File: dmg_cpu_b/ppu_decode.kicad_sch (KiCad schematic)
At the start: 39 parts

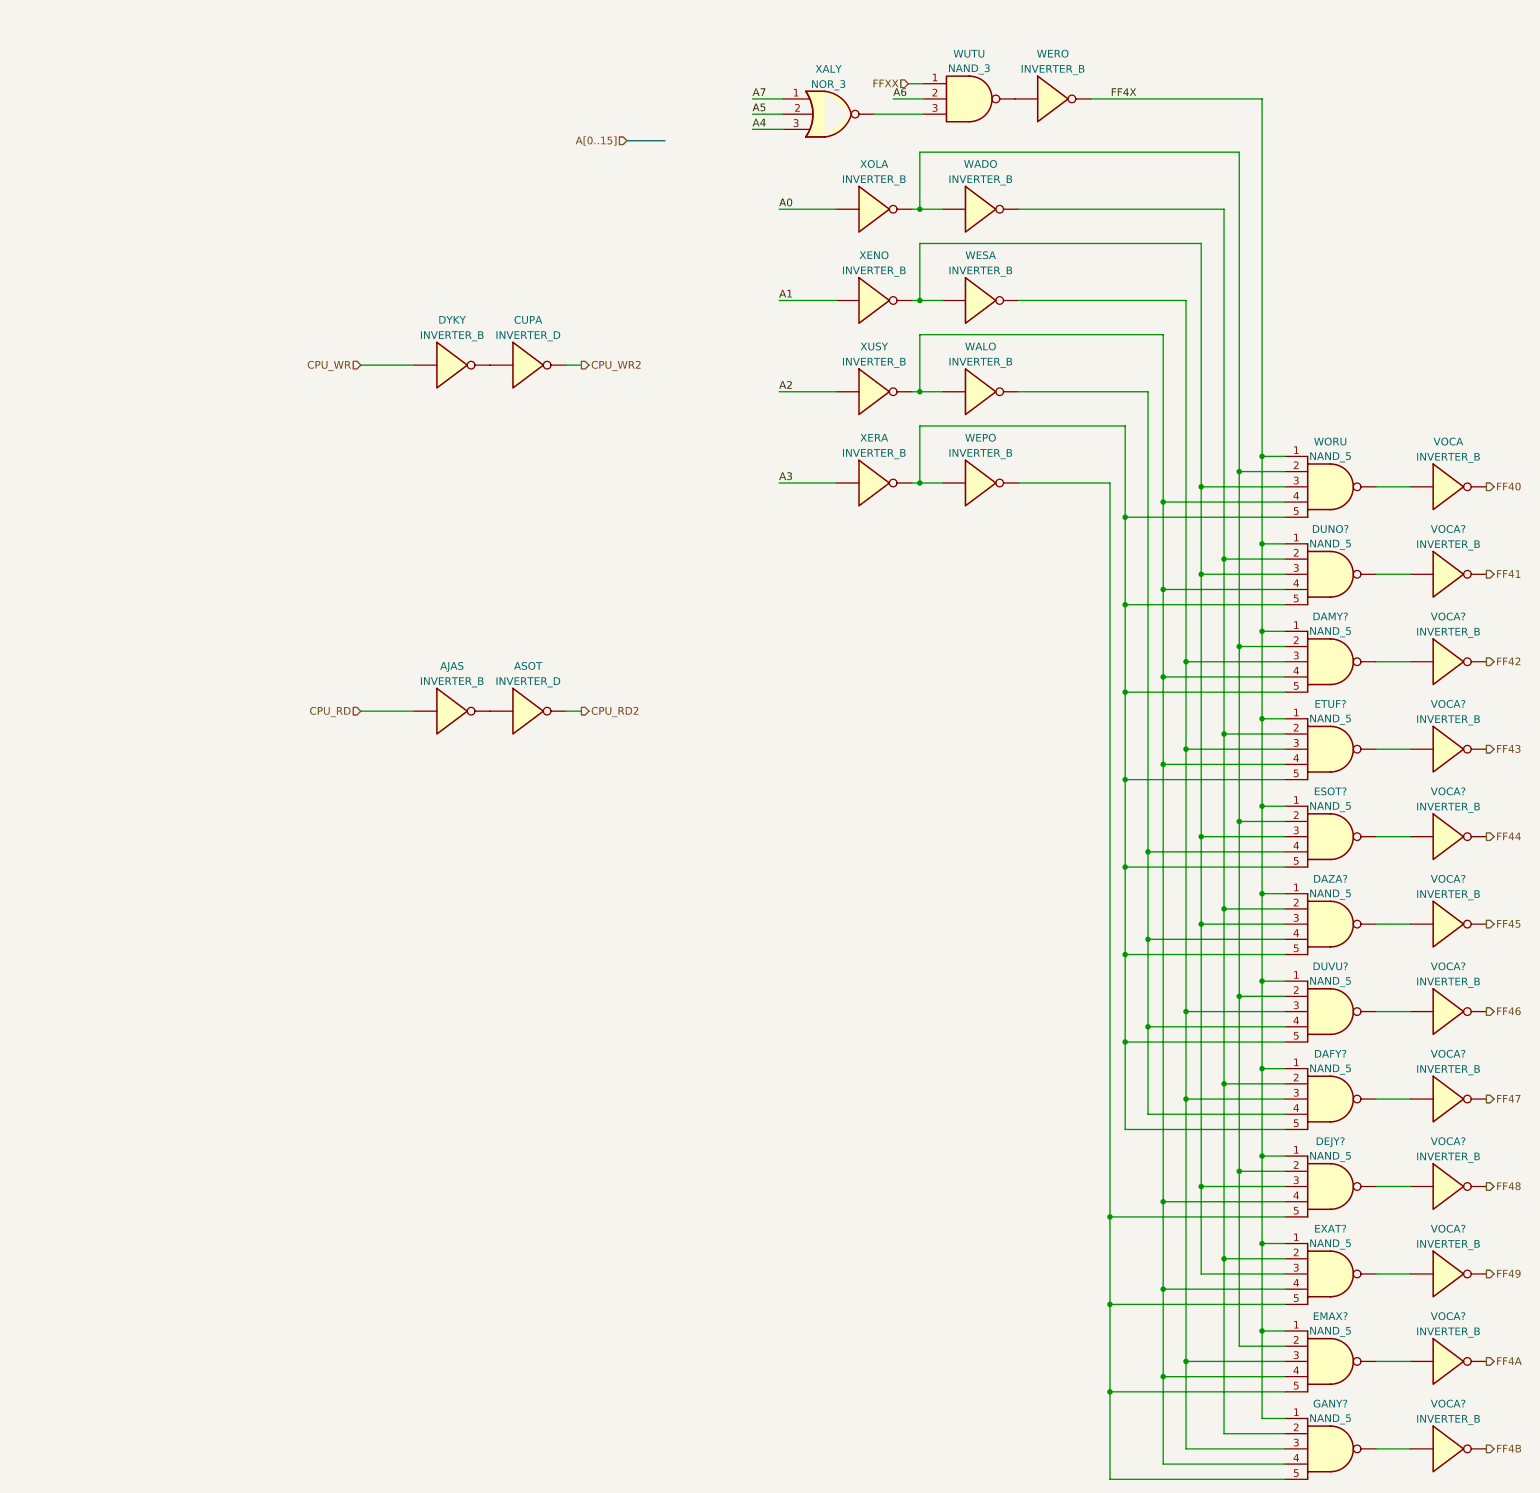
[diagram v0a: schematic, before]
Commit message: FF40,41,44,45 regs and LCD added
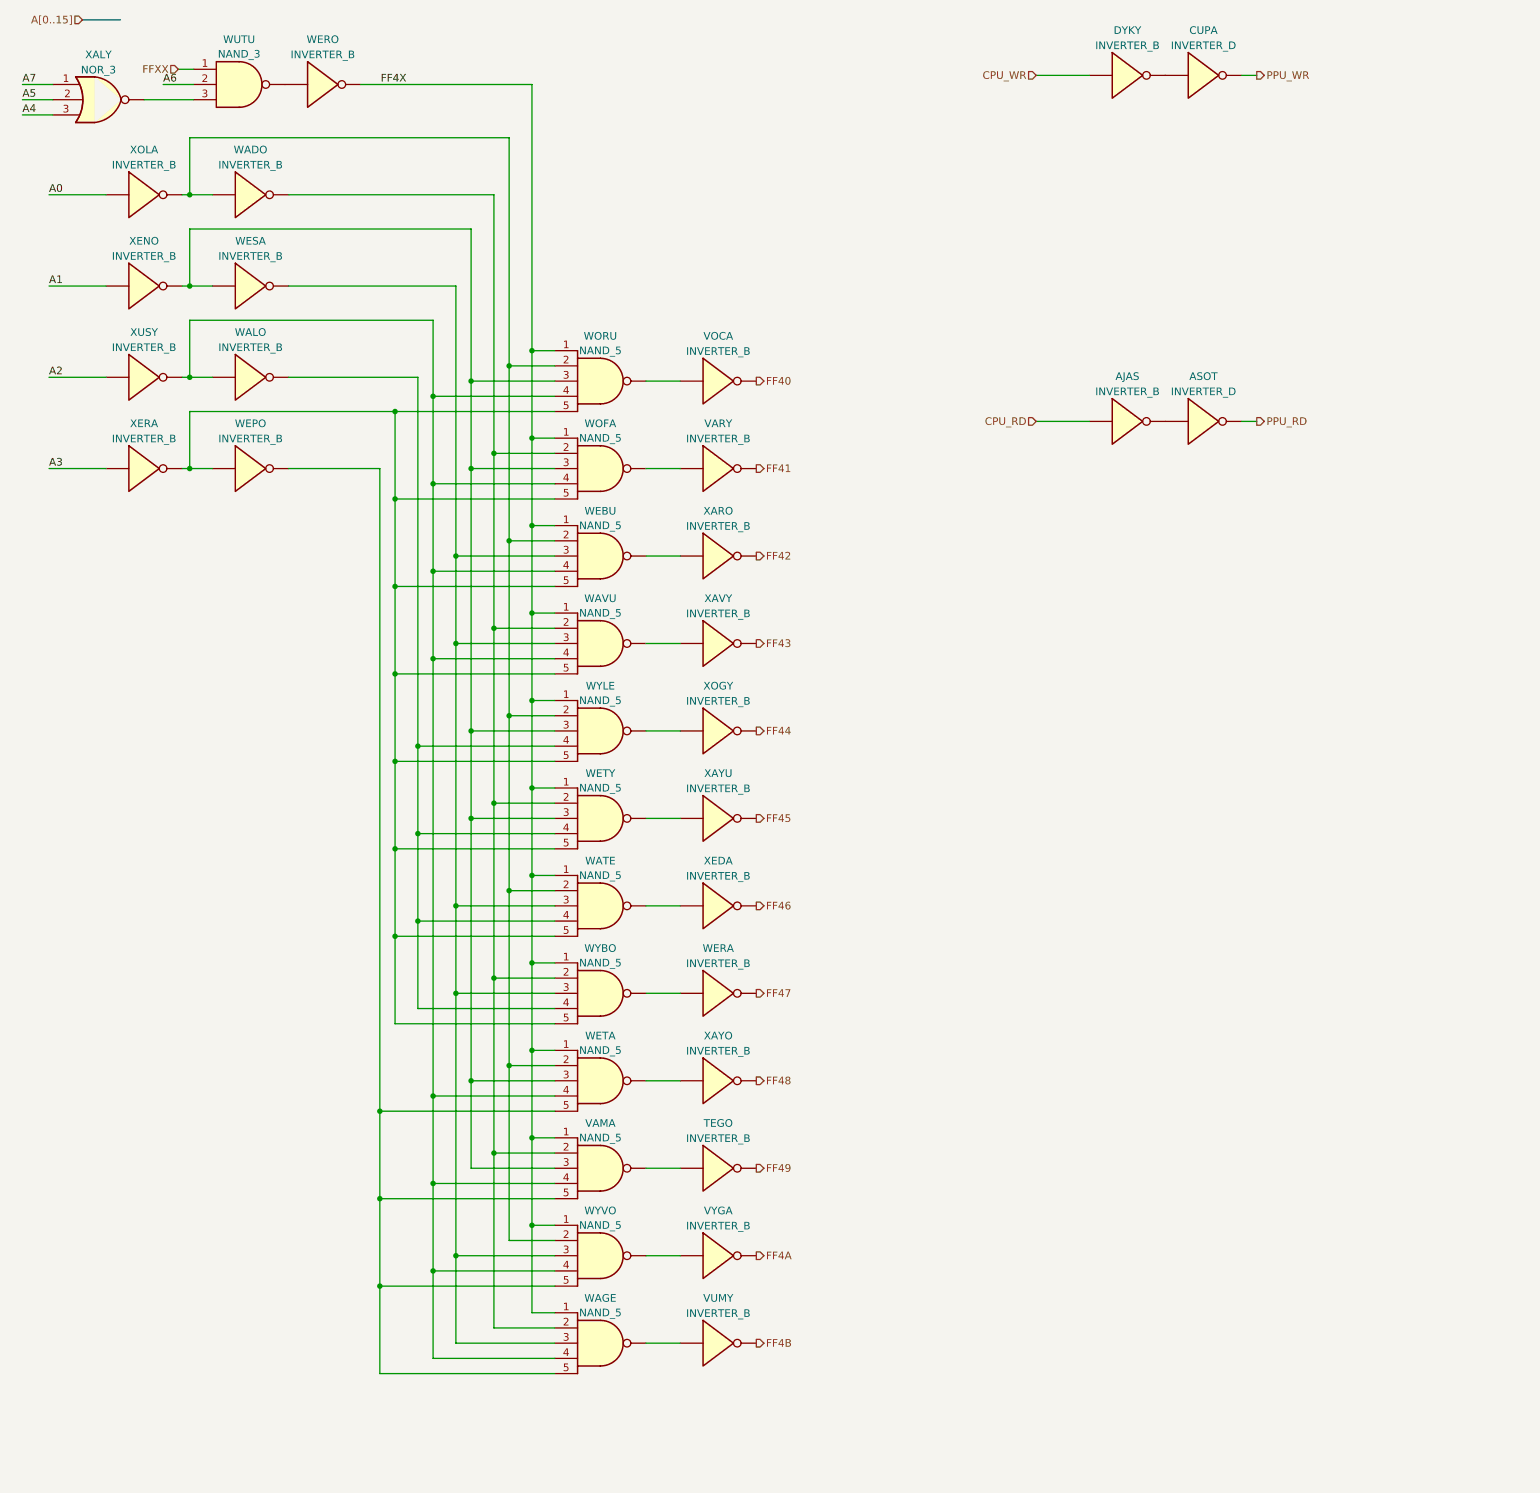
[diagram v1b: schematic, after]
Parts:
- gave numbers to parts that had none: 22
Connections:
- net CPU_RD2 renamed PPU_RD
- net CPU_WR2 renamed PPU_WR
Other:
- moved on the sheet: AJAS, ASOT, CUPA, DYKY, TEGO, VAMA, VARY, VOCA, VUMY, VYGA, WADO, WAGE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

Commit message: VRAM interface sheet added but various edits in existing sheets. Notable merge of RESET, CLOCKS and FF04 DIV sheets
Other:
- company: (none) -> CC-BY-SA-4.0 Régis Galland & Michael Singer -- Derived work from Furrtek
- title: (none) -> DMG CPU B
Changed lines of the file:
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@@
 (kicad_sch (version 20211123) (generator eeschema)
   (paper "A3")
+  (title_block
+    (title "DMG CPU B")
+    (date "2022-05-02")
+    (rev "0")
+    (company "CC-BY-SA-4.0 Régis Galland & Michael Singer -- Derived work from Furrtek")
+    (comment 1 "https://github.com/msinger/dmg-schematics")
+  )
   (junction (at 52.705 82.042) (diameter 0) (color 0 0 0 0)
   )

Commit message: Minor tweaks to help with clarity.
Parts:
- added CATY, DECY: INVERTER_A, symbol DMG_CPU_Cells:INVERTER_A
- added LEKO: INVERTER_B, symbol DMG_CPU_Cells:INVERTER_B
- added MYNU: NAND_2, symbol DMG_CPU_Cells:NAND_2
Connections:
- net PPU_RD: now also MYNU.2
- new net: CATY.1, DECY.2
- new net: LEKO.1, MYNU.3
- new net CPU_PHI2: DECY.1
- new net OAM_PHI: CATY.2, MYNU.1
- new net OAM_RD: LEKO.2
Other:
- moved on the sheet: AJAS, ASOT, CUPA, DYKY

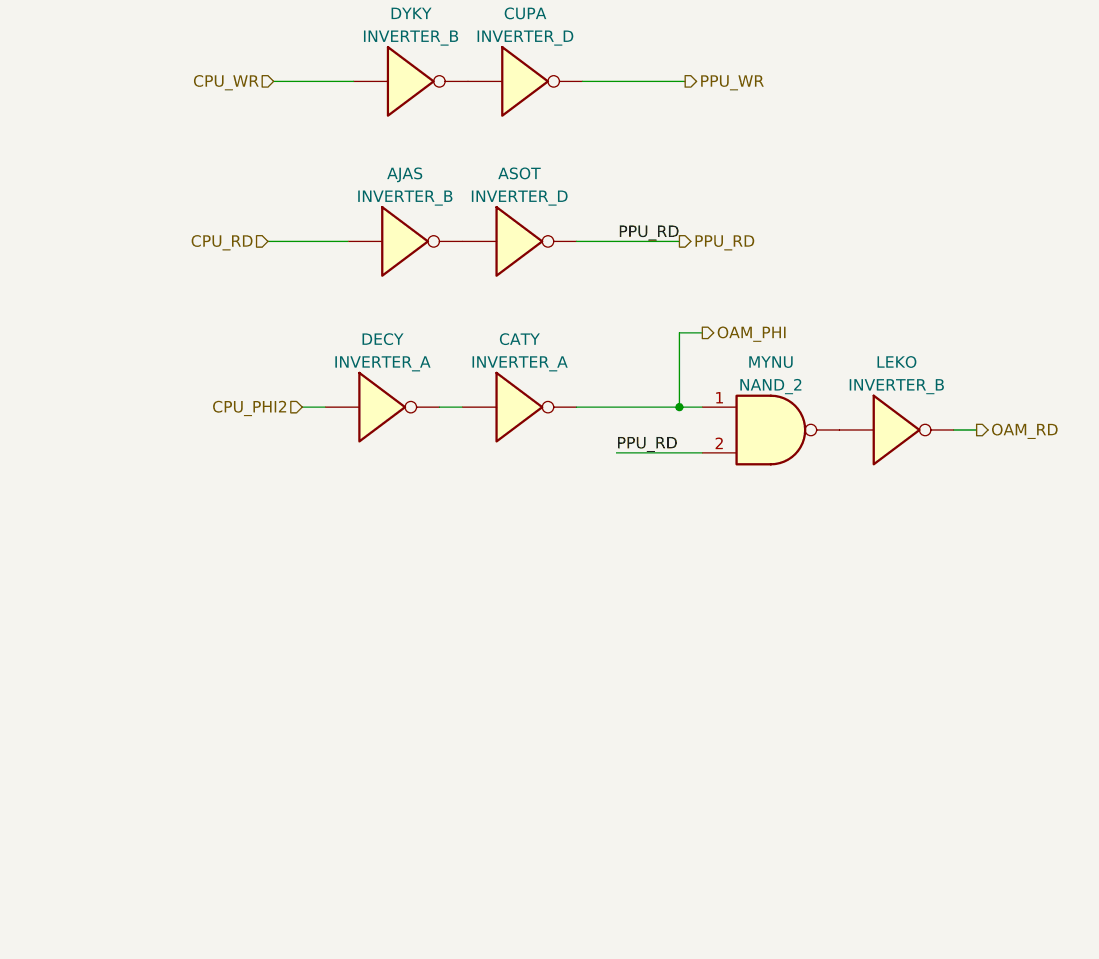
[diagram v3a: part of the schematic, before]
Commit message: OAM and sprite x priority sheets added. OAM sheet still needs some work on it.
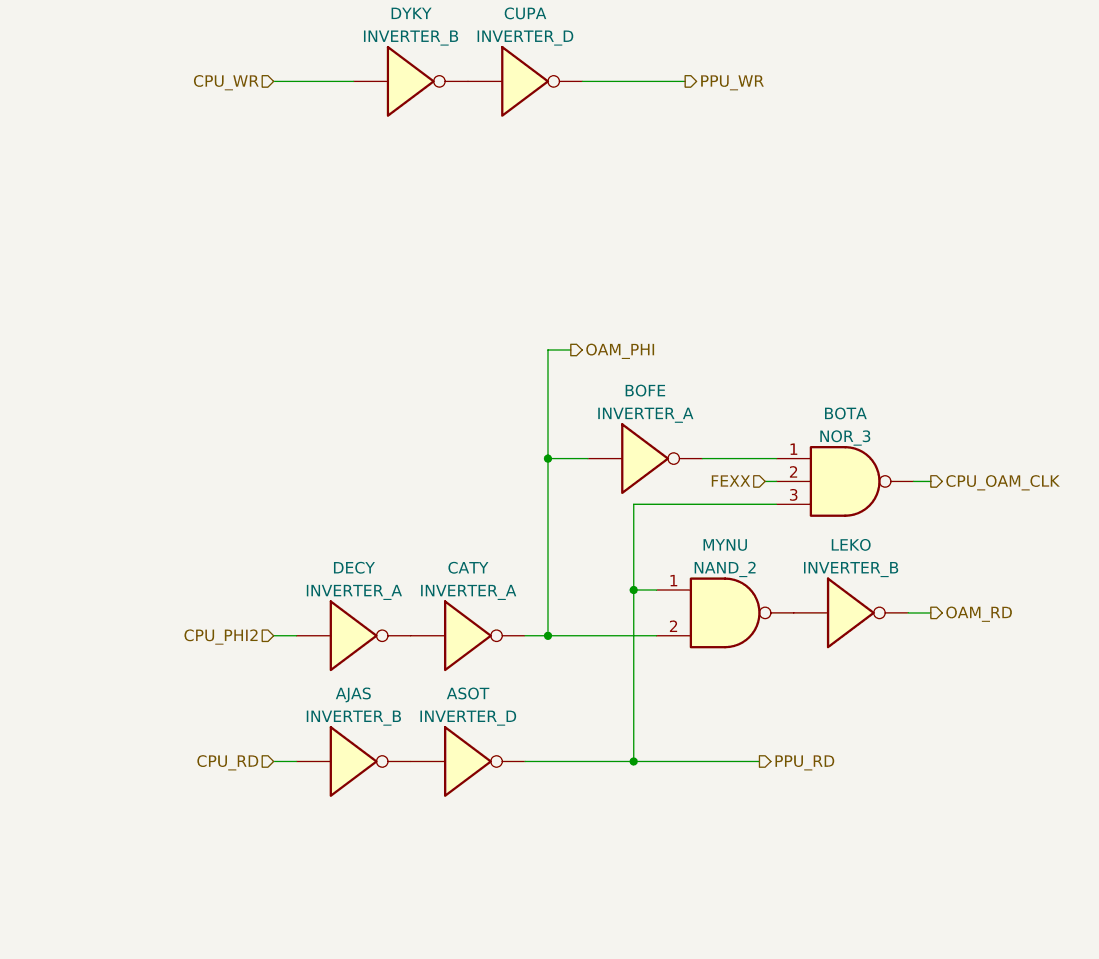
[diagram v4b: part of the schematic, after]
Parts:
- added BOFE: INVERTER_A, symbol DMG_CPU_Cells:INVERTER_A
- added BOTA: NOR_3, symbol DMG_CPU_Cells:NAND_3
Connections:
- net OAM_PHI: now also MYNU.2, BOFE.1; no longer MYNU.1
- net PPU_RD: now also MYNU.1, BOTA.3; no longer MYNU.2
- new net: BOFE.2, BOTA.1
- new net CPU_OAM_CLK: BOTA.4
- new net FEXX: BOTA.2
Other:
- moved on the sheet: AJAS, ASOT, CATY, DECY, LEKO, MYNU

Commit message: All sheets captured. Serious tidying is required in PPU section.
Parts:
- added ATAR, LYFE, LYHA, PYRY, WYCE, XARE, XEBE, XUCA: INVERTER_A, symbol DMG_CPU_Cells:INVERTER_A
- added VAHA, VATO, VOKE, WUKA, WYJU, WYPO, XEBU, XERO: TRI_INV_IF0, symbol DMG_CPU_Cells:TRI_INV_IF0
- added VYRE, WARU: AND_2, symbol DMG_CPU_Cells:AND_2
- added VYXE, WEXU, WOKY, WYMO, XAFO, XONA, XYLO, XYMO: DR_LATCH, symbol DMG_CPU_Cells:DR_LATCH
- added XAPO: INVERTER_B, symbol DMG_CPU_Cells:INVERTER_B
- added XECY: D_LATCH_A, symbol DMG_CPU_Cells:D_LATCH_A
- added XODO: NAND_2, symbol DMG_CPU_Cells:NAND_2
- added XUVA: DFFR_B2, symbol DMG_CPU_Cells:DFFR_B2
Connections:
- net FF40: now also VYRE.1, WARU.1
- net PPU_RD: now also VYRE.2
- net PPU_WR: now also WARU.2
- new net: XEBE.2, XECY.2 (D), XODO.2
- new net: XAPO.1, XODO.3
- new net: VYXE.1 (~{ENA}), VYXE.3 (ENA), WARU.3, WEXU.1 (~{ENA}), WEXU.3 (ENA), WOKY.1 (~{ENA}), WOKY.3 (ENA), WYMO.1 (~{ENA}), WYMO.3 (ENA), XAFO.1 (~{ENA}), XAFO.3 (ENA), XONA.1 (~{ENA}), XONA.3 (ENA), XUCA.1, XUVA.2 (~{RESET}), XUVA.4 (~{RESET}), XYLO.1 (~{ENA}), XYLO.3 (ENA), XYMO.1 (~{ENA}), XYMO.3 (ENA)
- new net: VYXE.4 (~{RESET}), WEXU.4 (~{RESET}), WOKY.4 (~{RESET}), WYMO.4 (~{RESET}), XAFO.4 (~{RESET}), XARE.2, XONA.4 (~{RESET}), XYLO.4 (~{RESET}), XYMO.4 (~{RESET})
- new net: VAHA.2, WOKY.6 (~{Q})
- new net: VYRE.3, WYCE.1
- new net: VAHA.1 (~{ENA}), VATO.1 (~{ENA}), VOKE.1 (~{ENA}), WUKA.1 (~{ENA}), WYCE.2, WYJU.1 (~{ENA}), WYPO.1 (~{ENA}), XEBU.1 (~{ENA}), XERO.1 (~{ENA})
- new net: XECY.4 (Q), XUVA.3 (D)
- new net: XECY.1 (~{ENA}), XECY.3 (ENA), XUCA.2
- new net: XEBU.2, XONA.6 (~{Q})
- new net: VOKE.2, WEXU.6 (~{Q})
- new net: WUKA.2, XAFO.6 (~{Q})
- new net: XERO.2, XYLO.6 (~{Q})
- new net: VYXE.6 (~{Q}), WYPO.2
- new net: WYJU.2, XYMO.6 (~{Q})
- new net: VATO.2, WYMO.6 (~{Q})
- new net D0: VYXE.2 (D), WYPO.3
- new net D1: XERO.3, XYLO.2 (D)
- new net D2: WYJU.3, XYMO.2 (D)
- new net D3: WUKA.3, XAFO.2 (D)
- new net D4: VOKE.3, WEXU.2 (D)
- new net D5: VATO.3, WYMO.2 (D)
- new net D6: VAHA.3, WOKY.2 (D)
- new net D7: XEBU.3, XONA.2 (D)
- new net FF40_D0: VYXE.5 (Q)
- new net FF40_D1: XYLO.5 (Q)
- new net FF40_D2: XYMO.5 (Q)
- new net FF40_D3: XAFO.5 (Q)
- new net FF40_D4: WEXU.5 (Q)
- new net FF40_D5: WYMO.5 (Q)
- new net FF40_D6: WOKY.5 (Q)
- new net FF40_D7: XODO.1, XONA.5 (Q)
- new net RESET7: XARE.1, XEBE.1
- new net RESET_VIDEO: ATAR.2
- new net RESET_VIDEO2: PYRY.2
- new net RESET_VIDEO3: LYFE.1, LYHA.2
- new net ~{DMA_PHI2}: XUVA.1 (CLK)
- new net ~{RESET_VIDEO2}: LYFE.2
- new net ~{RESET_VIDEO}: ATAR.1, LYHA.1, PYRY.1, XAPO.2
- no-connect marks 0 -> 3
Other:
- note added: "FF40 LDLC"
- moved on the sheet: AJAS, ASOT, BOFE, BOTA, CATY, CUPA, DECY, DYKY, LEKO, MYNU, TEGO, VAMA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

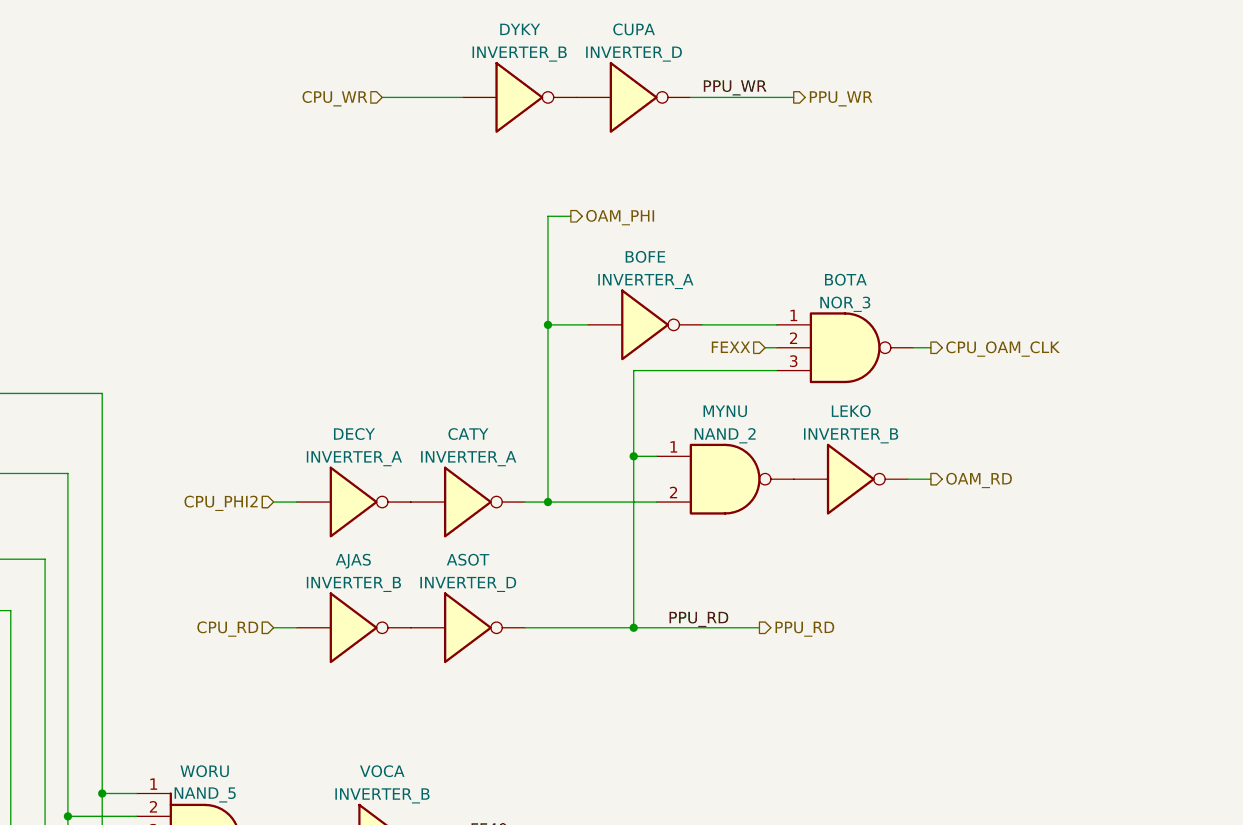
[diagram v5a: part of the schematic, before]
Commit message: Changes made based on review. PPU hierarchcal sheet work started.
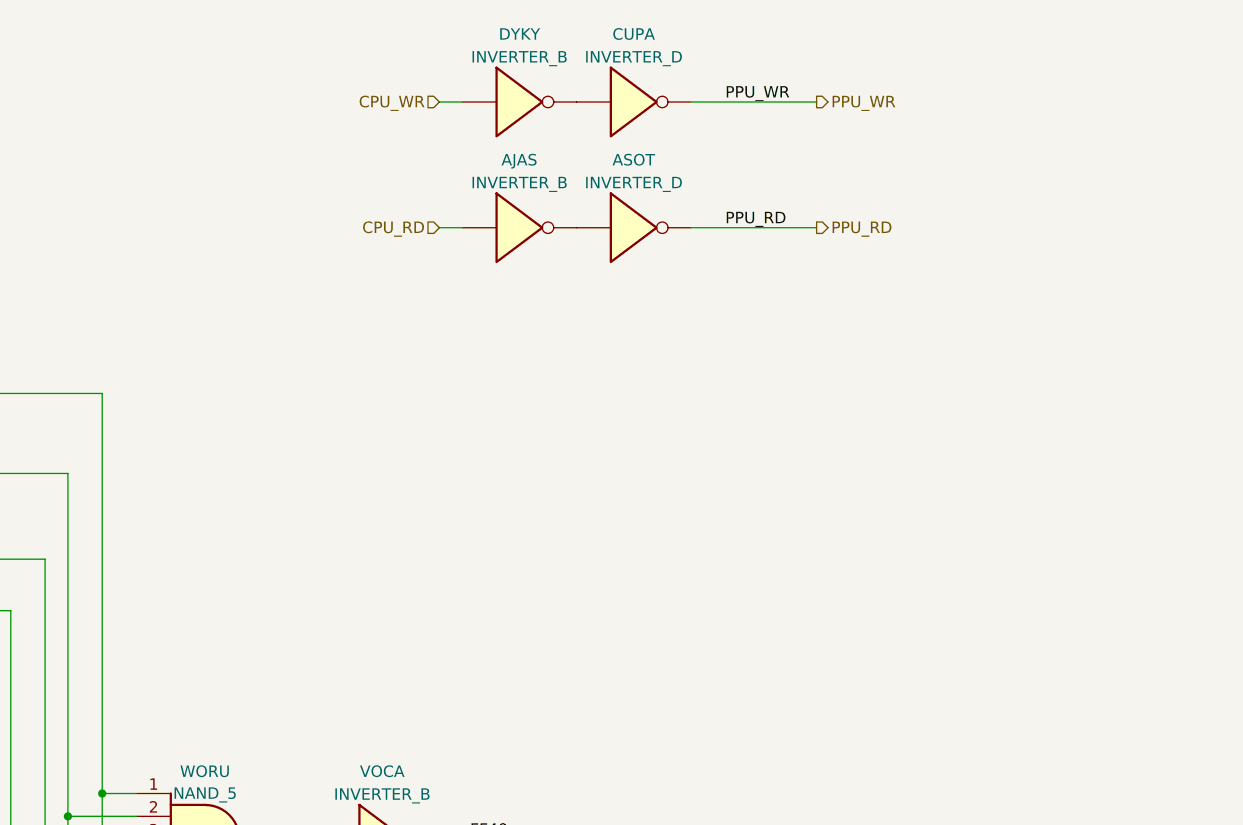
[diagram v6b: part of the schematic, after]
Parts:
- removed BOFE, CATY, DECY: INVERTER_A, symbol DMG_CPU_Cells:INVERTER_A
- removed BOTA: NOR_3, symbol DMG_CPU_Cells:NAND_3
- removed LEKO: INVERTER_B, symbol DMG_CPU_Cells:INVERTER_B
- removed MYNU: NAND_2, symbol DMG_CPU_Cells:NAND_2
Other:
- moved on the sheet: AJAS, ASOT, CUPA, DYKY
